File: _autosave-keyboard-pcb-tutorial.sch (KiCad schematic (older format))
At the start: 24 parts

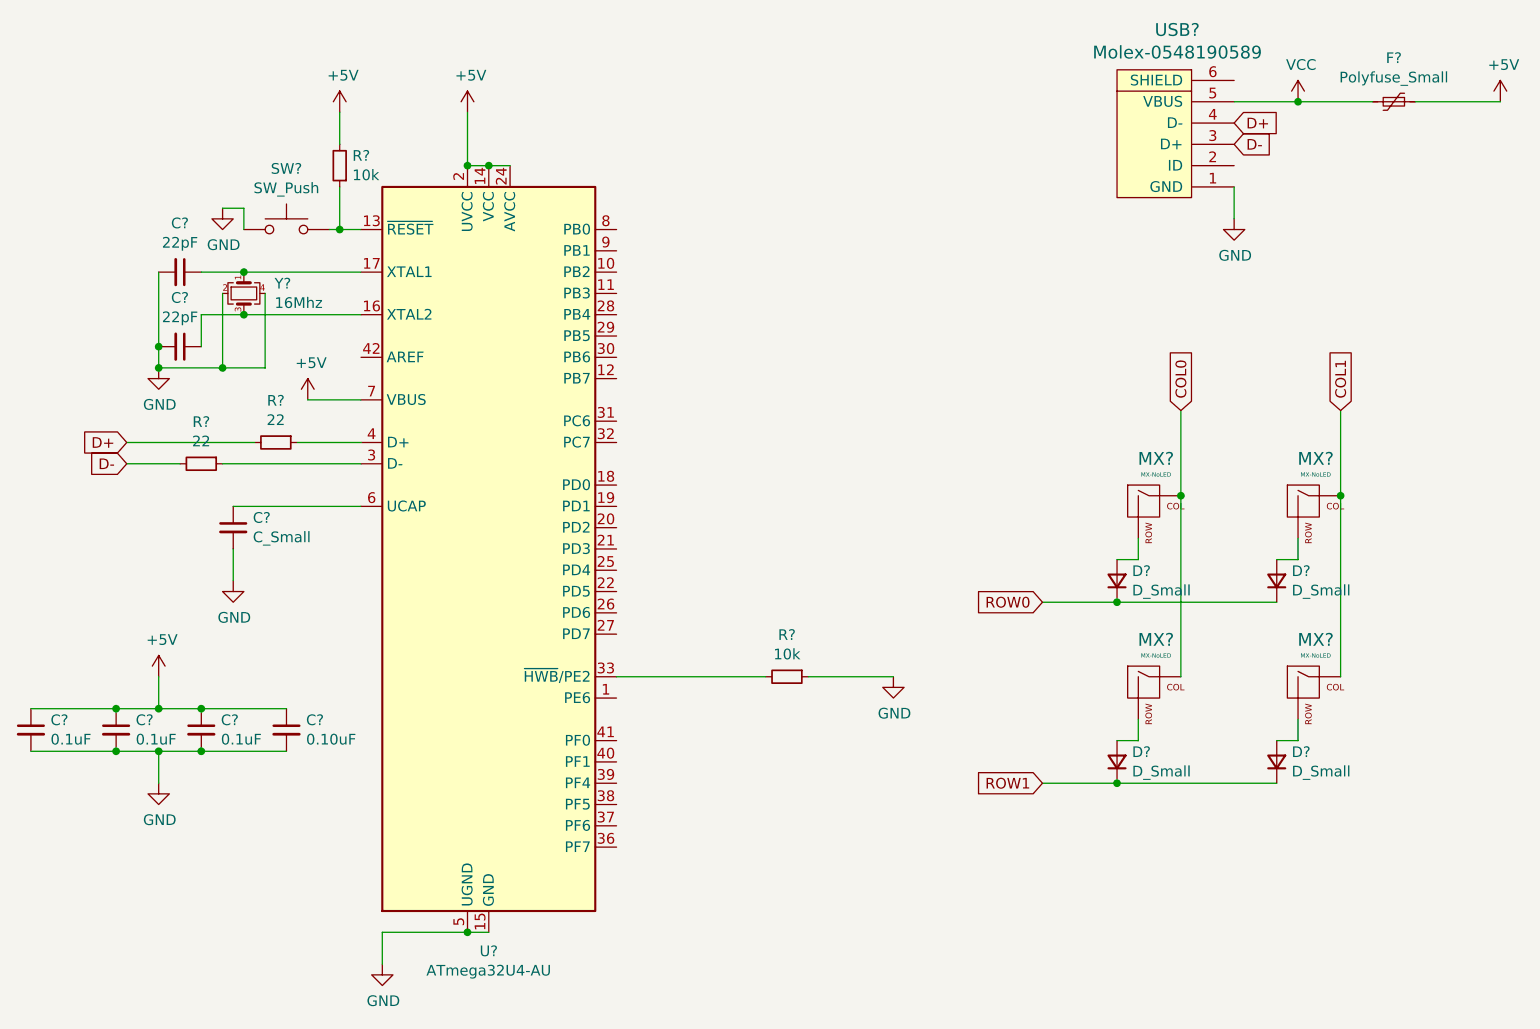
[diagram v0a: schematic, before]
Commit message: PCB footprints
Assigned PCB footprints
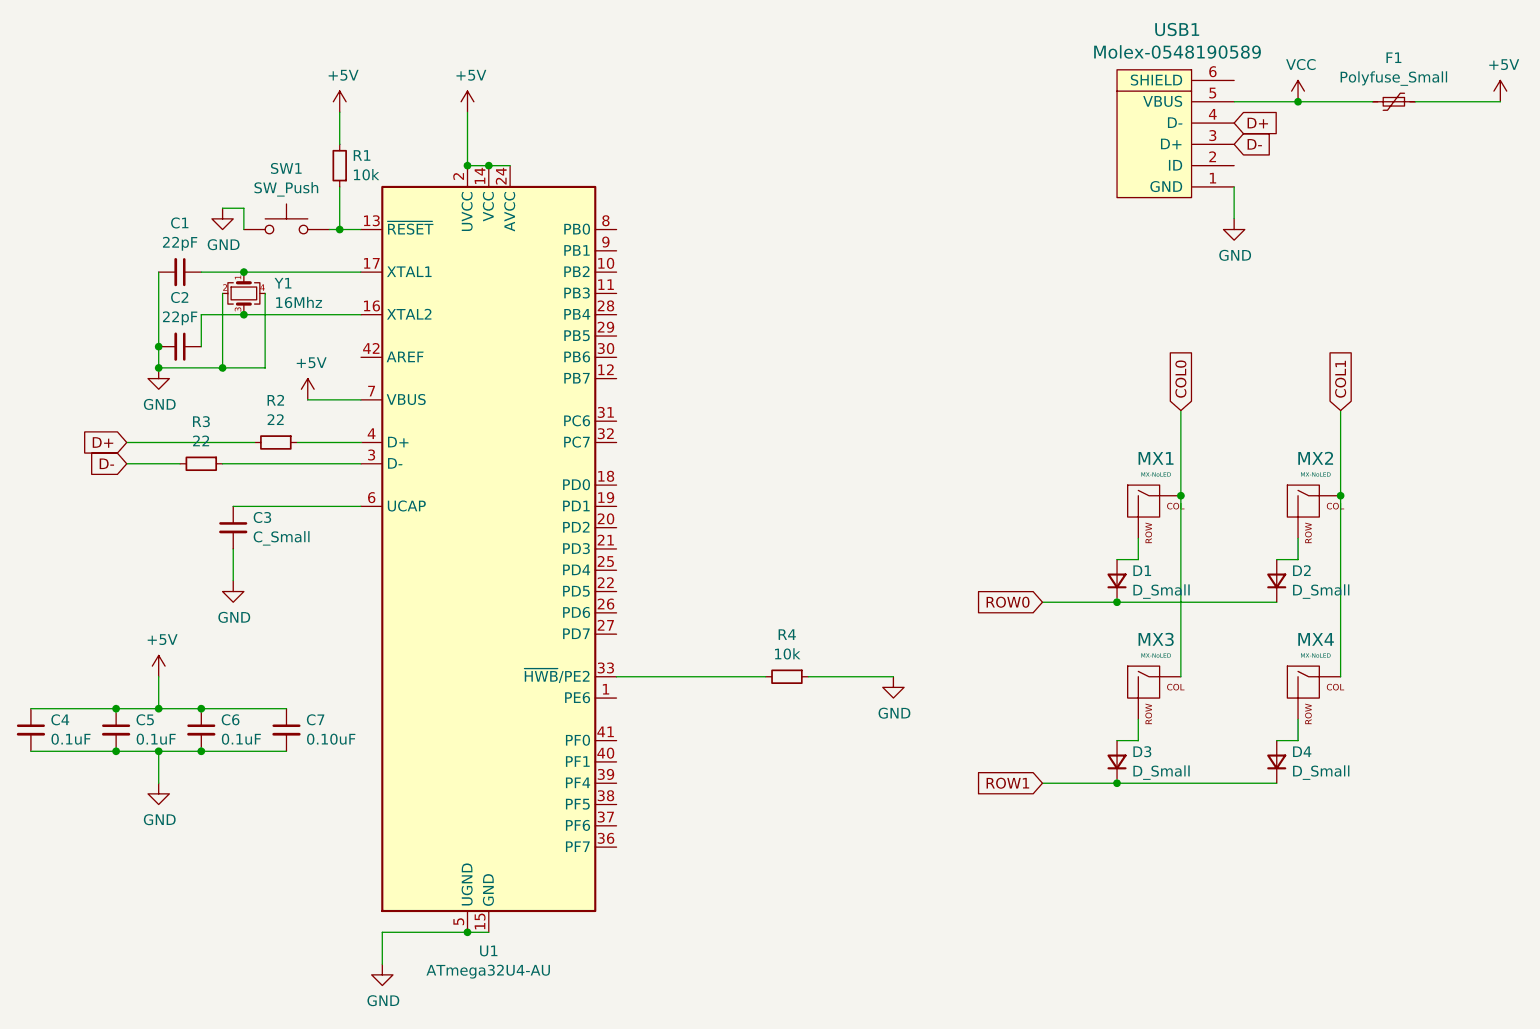
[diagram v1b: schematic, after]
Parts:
- C1, C2, C3, C4, C5, C6, C7: renamed from C?; footprint (none) -> Capacitor_SMD:C_0805_2012Metric
- D1, D2, D3, D4: renamed from D?; footprint (none) -> Diode_SMD:D_SOD-123
- F1: renamed from F?; footprint (none) -> Fuse:Fuse_1206_3216Metric
- R1, R2, R3, R4: renamed from R?; footprint (none) -> Resistor_SMD:R_0805_2012Metric
- SW1: renamed from SW?; footprint (none) -> random-keyboard-parts:SKQG-1155865
- USB1: renamed from USB?; footprint (none) -> random-keyboard-parts:Molex-0548190589
- Y1: renamed from Y?; footprint (none) -> Crystal:Crystal_SMD_3225-4Pin_3.2x2.5mm
- gave numbers to parts that had none: 5
